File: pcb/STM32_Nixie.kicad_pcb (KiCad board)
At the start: 4 copper layers, 154 x 57 mm, 189 parts, among them J1 CON_SAMTEC_14P_2R_1m27_P_KEY_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, J2 CONN_USBC_RCPT_USB2.0_USB4085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, Q1 NFET_250V_10A_TPH1110FNH,L1Q, Q2 NFET_60V_0A5_2N7002KT1G, SW1 ENC_SPST_24PPR_PEC12R-4225F-S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, U1 IC_SR_MC_HV5622PG-G, U2 IC_SR_MC_HV5622PG-G, U3 IC_MCU_STM32F100C4T6B_48LQFP, U4 IC_LVL_ONSEMI_MC14504BDTR2G, U5 REG_SW_BOOST_TI_TLV61046ADBV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

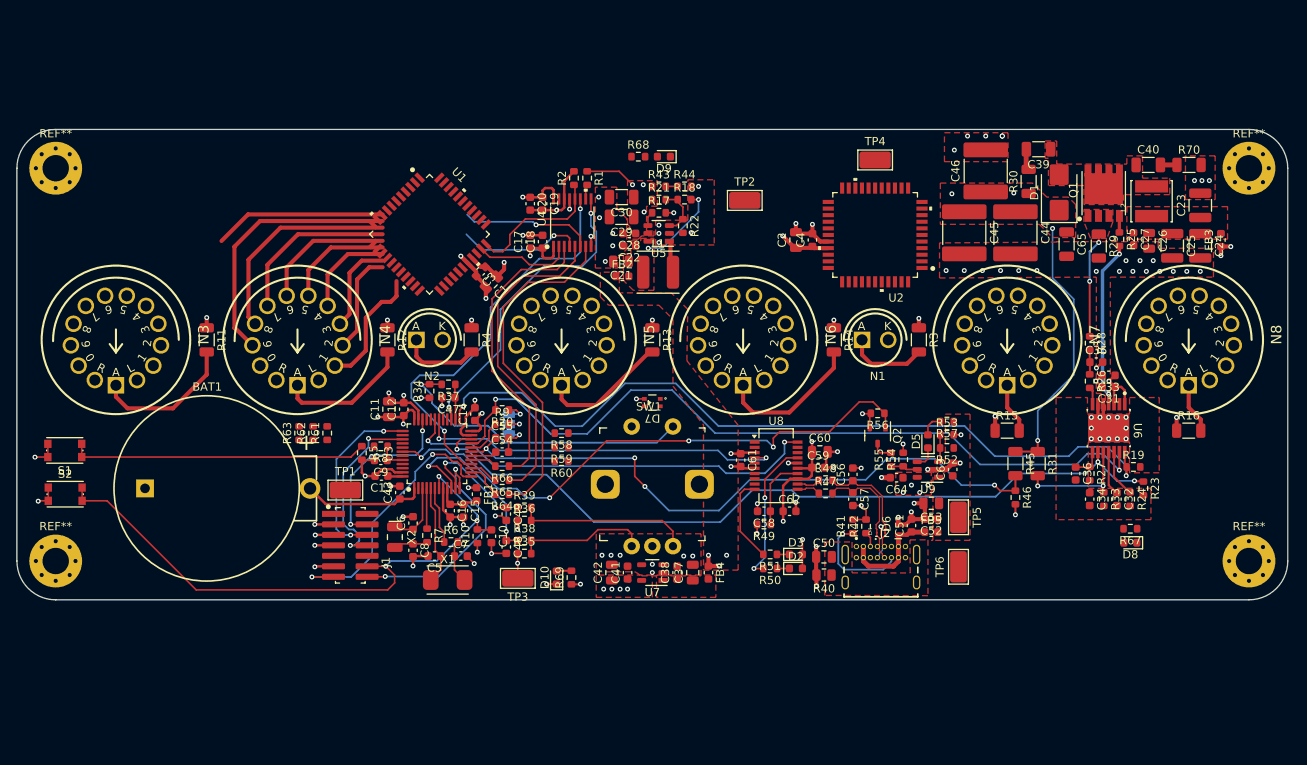
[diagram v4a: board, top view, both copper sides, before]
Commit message: Reshuffled nixie schematic to ease with routing. Need to fix the other 3 digits next.
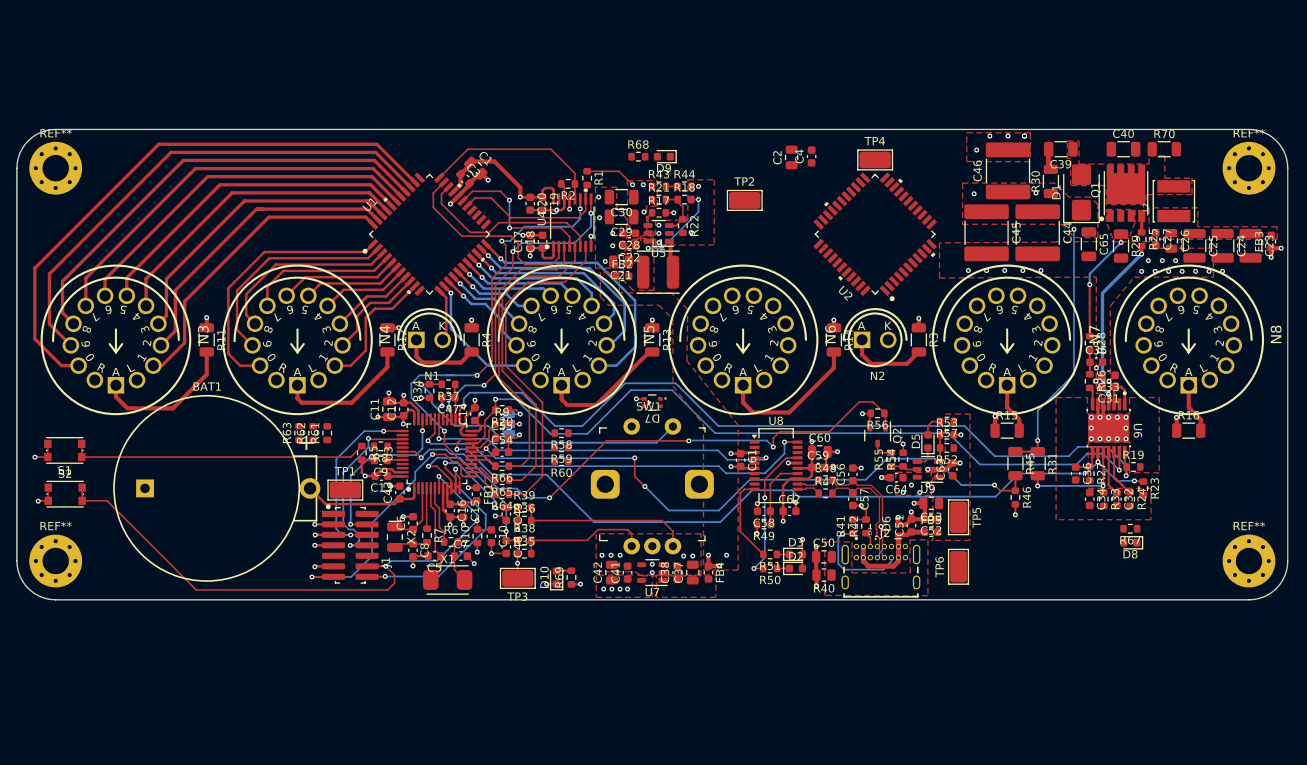
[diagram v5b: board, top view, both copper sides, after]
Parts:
- moved C1 13.9 mm to (130.6, 66.2), turned to -45 degrees
- moved C3 11.4 mm to (129.3, 67.5), turned to -45 degrees
- moved C4 10.1 mm to (171.3, 64.8)
- moved C2 10.0 mm to (168.9, 64.9)
- moved C23 7.82 mm to (224.5, 75.6), turned to -90 degrees
- moved FB3 6.10 mm to (227.0, 75.1)
- moved C40 3.55 mm to (209.1, 63.9)
- moved R70 3.55 mm to (214.0, 63.9)
- moved C26 2.70 mm to (214.9, 75.0)
- moved C65 2.70 mm to (204.9, 75.4)
- moved Q1 2.70 mm to (209.4, 69.2)
- moved R25 2.70 mm to (211.3, 74.8)
- moved R29 2.70 mm to (208.8, 75.6)
- moved R30 2.70 mm to (200.3, 67.8)
- moved C24 2.70 mm to (221.1, 75.6)
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- renumbered N2 to N1, N1 to N2
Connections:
- N1 pad A: /Nixie Display/DOT2_A -> /Nixie Display/DOT1_A
- N1 pad K: /Nixie Display/DOT2 -> /Nixie Display/DOT1
- N2 pad A: /Nixie Display/DOT1_A -> /Nixie Display/DOT2_A
- N2 pad K: /Nixie Display/DOT1 -> /Nixie Display/DOT2
- R3 pad 2: /Nixie Display/DOT1_A -> /Nixie Display/DOT2_A
- R4 pad 2: /Nixie Display/DOT2_A -> /Nixie Display/DOT1_A
- U1 pad 1: /Nixie Display/M1_2 -> /Nixie Display/H2_0
- U1 pad 10: /Nixie Display/H2_3 -> /Nixie Display/H2_1
- U1 pad 11: /Nixie Display/H2_2 -> unconnected-(U1-HVOUT12-Pad11)
- U1 pad 12: /Nixie Display/H2_1 -> /Nixie Display/DOT1
- U1 pad 13: /Nixie Display/H1_0 -> /Nixie Display/M1_0
- U1 pad 14: /Nixie Display/H1_9 -> /Nixie Display/M1_9
- U1 pad 15: /Nixie Display/H1_8 -> /Nixie Display/M1_8
- U1 pad 16: /Nixie Display/H1_7 -> /Nixie Display/M1_7
- U1 pad 17: /Nixie Display/H1_6 -> /Nixie Display/M1_6
- U1 pad 18: /Nixie Display/H1_5 -> /Nixie Display/M1_5
- U1 pad 19: /Nixie Display/H1_4 -> /Nixie Display/M1_4
- U1 pad 2: /Nixie Display/M1_1 -> /Nixie Display/H2_9
- U1 pad 20: /Nixie Display/H1_3 -> /Nixie Display/M1_3
- U1 pad 21: /Nixie Display/H1_2 -> /Nixie Display/M1_2
- U1 pad 22: /Nixie Display/H1_1 -> /Nixie Display/M1_1
- U1 pad 3: /Nixie Display/H2_0 -> /Nixie Display/H2_8
- U1 pad 35: /Nixie Display/M2_2 -> /Nixie Display/H1_0
- U1 pad 36: /Nixie Display/M2_1 -> /Nixie Display/H1_9
- U1 pad 37: /Nixie Display/M1_0 -> /Nixie Display/H1_8
- U1 pad 38: /Nixie Display/M1_9 -> /Nixie Display/H1_7
- U1 pad 39: /Nixie Display/M1_8 -> /Nixie Display/H1_6
- U1 pad 4: /Nixie Display/H2_9 -> /Nixie Display/H2_7
- U1 pad 40: /Nixie Display/M1_7 -> /Nixie Display/H1_5
- U1 pad 41: /Nixie Display/M1_6 -> /Nixie Display/H1_4
- U1 pad 42: /Nixie Display/M1_5 -> /Nixie Display/H1_3
- U1 pad 43: /Nixie Display/M1_4 -> /Nixie Display/H1_2
- U1 pad 44: /Nixie Display/M1_3 -> /Nixie Display/H1_1
- U1 pad 5: /Nixie Display/H2_8 -> /Nixie Display/H2_6
- U1 pad 6: /Nixie Display/H2_7 -> /Nixie Display/H2_5
- U1 pad 7: /Nixie Display/H2_6 -> /Nixie Display/H2_4
- U1 pad 8: /Nixie Display/H2_5 -> /Nixie Display/H2_3
- U1 pad 9: /Nixie Display/H2_4 -> /Nixie Display/H2_2
- U2 pad 1: /Nixie Display/S2_4 -> /Nixie Display/S2_2
- U2 pad 10: /Nixie Display/S1_5 -> /Nixie Display/S1_3
- U2 pad 11: /Nixie Display/S1_4 -> /Nixie Display/S1_2
- U2 pad 12: /Nixie Display/S1_3 -> /Nixie Display/S1_1
- U2 pad 13: /Nixie Display/S1_2 -> /Nixie Display/M2_0
- U2 pad 14: /Nixie Display/S1_1 -> /Nixie Display/M2_9
- U2 pad 15: /Nixie Display/M2_0 -> /Nixie Display/M2_8
- U2 pad 16: /Nixie Display/M2_9 -> /Nixie Display/M2_7
- U2 pad 17: /Nixie Display/M2_8 -> /Nixie Display/M2_6
- U2 pad 18: /Nixie Display/M2_7 -> /Nixie Display/M2_5
- U2 pad 19: /Nixie Display/M2_6 -> /Nixie Display/M2_4
- U2 pad 2: /Nixie Display/S2_3 -> /Nixie Display/S2_1
- U2 pad 20: /Nixie Display/M2_5 -> /Nixie Display/M2_3
- U2 pad 21: /Nixie Display/M2_4 -> /Nixie Display/M2_2
- U2 pad 22: /Nixie Display/M2_3 -> /Nixie Display/M2_1
- U2 pad 3: /Nixie Display/S2_2 -> /Nixie Display/S1_0
- U2 pad 35: unconnected-(U2-HVOUT32-Pad35) -> /Nixie Display/DOT2
- U2 pad 37: /Nixie Display/DOT2 -> /Nixie Display/S2_0
- U2 pad 38: /Nixie Display/DOT1 -> /Nixie Display/S2_9
- U2 pad 39: /Nixie Display/S2_0 -> /Nixie Display/S2_8
- U2 pad 4: /Nixie Display/S2_1 -> /Nixie Display/S1_9
- U2 pad 40: /Nixie Display/S2_9 -> /Nixie Display/S2_7
- U2 pad 41: /Nixie Display/S2_8 -> /Nixie Display/S2_6
- U2 pad 42: /Nixie Display/S2_7 -> /Nixie Display/S2_5
- U2 pad 43: /Nixie Display/S2_6 -> /Nixie Display/S2_4
- U2 pad 44: /Nixie Display/S2_5 -> /Nixie Display/S2_3
- U2 pad 5: /Nixie Display/S1_0 -> /Nixie Display/S1_8
- U2 pad 6: /Nixie Display/S1_9 -> /Nixie Display/S1_7
- U2 pad 7: /Nixie Display/S1_8 -> /Nixie Display/S1_6
- U2 pad 8: /Nixie Display/S1_7 -> /Nixie Display/S1_5
- U2 pad 9: /Nixie Display/S1_6 -> /Nixie Display/S1_4
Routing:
- net /Nixie Display/H1_0: track 0.00 -> 69.4 mm
- net /Nixie Display/H1_9: track 0.00 -> 61.3 mm
- net /Nixie Display/H1_8: track 0.00 -> 54.9 mm
- net /Nixie Display/H1_7: track 0.00 -> 48.5 mm
- net /Nixie Display/H1_6: track 0.00 -> 43.7 mm
- net /Nixie Display/H1_5: track 0.00 -> 40.0 mm
- net /Nixie Display/H1_4: track 0.00 -> 37.7 mm
- net /Nixie Display/H1_1: track 0.00 -> 37.4 mm
- net /Nixie Display/H1_2: track 0.00 -> 36.9 mm
- net /Nixie Display/H1_3: track 0.00 -> 36.6 mm
- net /Nixie Display/M1_1: track 0.00 -> 31.8 mm, vias 0 -> 1
- net /Nixie Display/M1_2: track 0.00 -> 26.4 mm, vias 0 -> 1
- net /Nixie Display/M1_3: track 0.00 -> 22.1 mm, vias 0 -> 1
- net /Nixie Display/M1_4: track 0.00 -> 17.8 mm, vias 0 -> 1
- net /nPOL_12V: track 1.77 -> 19.3 mm
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
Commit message: Reshuffled Nixie page some more to make routing cleaner
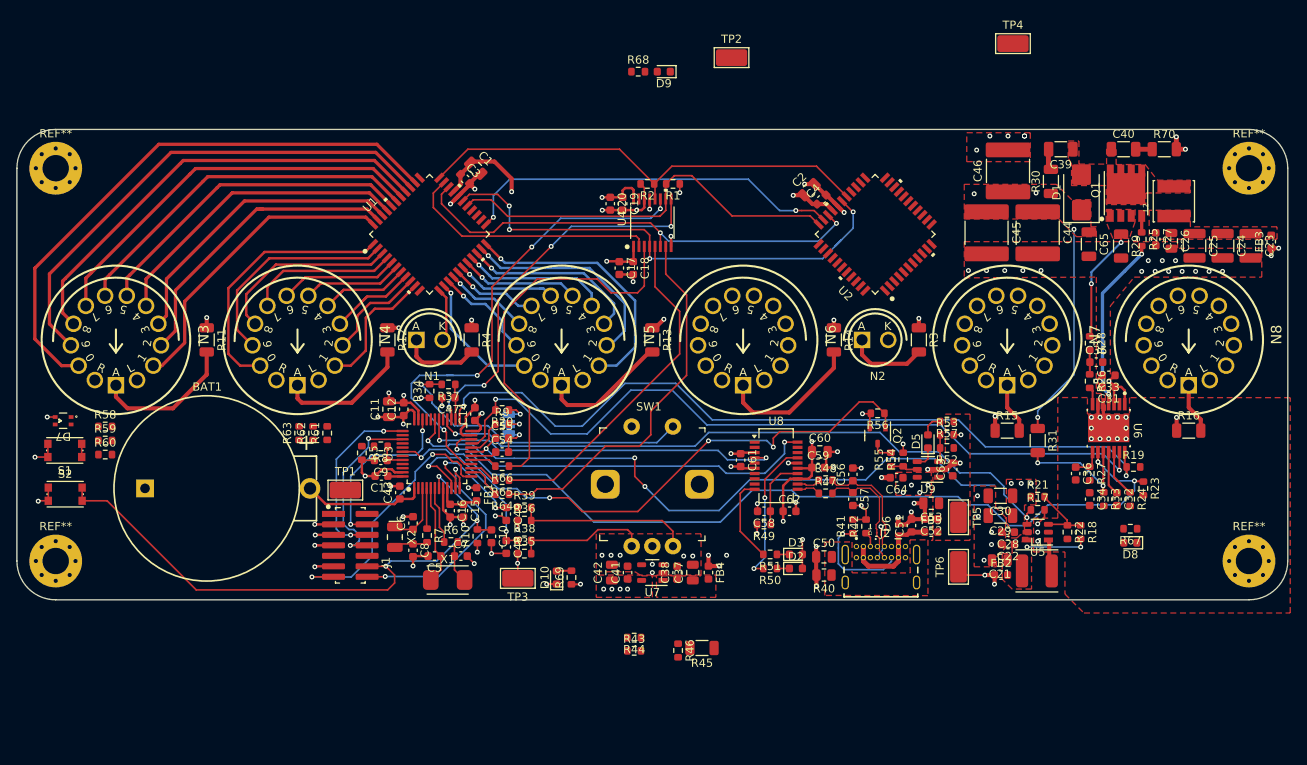
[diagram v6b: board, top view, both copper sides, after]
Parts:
- moved D7 71.4 mm to (80.6, 96.8)
- moved R18 62.7 mm to (203.9, 110.3), turned to -90 degrees
- moved R22 59.6 mm to (202.3, 110.3)
- moved U5 58.5 mm to (198.7, 110.3)
- moved C28 58.5 mm to (195.1, 110.3)
- moved C21 58.5 mm to (194.1, 113.7)
- moved C22 58.5 mm to (195.1, 111.8)
- moved C29 58.5 mm to (194.2, 108.3)
- moved C30 58.5 mm to (194.2, 105.9)
- moved L1 58.5 mm to (198.6, 115.0)
- moved FB2 58.5 mm to (194.3, 115.5)
- moved R17 58.3 mm to (198.7, 107.6)
- moved R21 58.3 mm to (198.7, 106.0)
- moved R43 56.4 mm to (149.8, 124.7)
- moved R58 55.3 mm to (85.7, 97.5), turned to 0 degrees
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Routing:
- net +12V: track 120.8 -> 31.6 mm, vias 5 -> 8
- net /MCU/EN_12V: track 1.76 -> 79.6 mm, vias 0 -> 2
- net /Nixie Display/DATA_CHAIN: track 0.00 -> 46.7 mm, vias 0 -> 2
- net /SPI_SCK_12V: track 18.9 -> 62.1 mm, vias 2 -> 4
- net /PWM_nBL_12V: track 22.2 -> 56.8 mm
- net /MCU/BOOT0_SW: track 36.1 -> 1.60 mm
- net /SPI_nCS_nLE_12V: track 23.0 -> 57.1 mm, vias 0 -> 2
- net /nPOL_12V: track 19.3 -> 50.0 mm
- net /SPI_PICO_3V3: track 35.9 -> 46.3 mm
- net GND: track 128.1 -> 136.5 mm
- net /MCU/DITHOFF_180V: track 95.3 -> 102.4 mm
- net /SPI_PICO_12V: track 24.4 -> 31.0 mm
- net /PWM_nBL_3V3: track 53.4 -> 59.5 mm
- net /nPOL_3V3: track 40.7 -> 46.4 mm
- net +5V: track 4.94 -> 10.3 mm, vias 9 -> 11
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
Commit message: All nets routed!! (I think)
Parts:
- moved R45 40.4 mm to (183.4, 92.9)
- moved R46 39.8 mm to (179.1, 92.9), turned to 180 degrees
- moved TP4 35.3 mm to (162.8, 64.0)
- moved R43 30.1 mm to (153.6, 94.8), turned to 180 degrees
- moved R44 28.3 mm to (150.4, 94.8)
- moved TP2 25.6 mm to (142.7, 70.0)
- moved D9 22.0 mm to (137.8, 70.0), turned to -90 degrees
- moved R68 18.9 mm to (139.5, 70.0), turned to -90 degrees
- moved D8 12.5 mm to (219.4, 103.4)
- moved R67 9.03 mm to (216.2, 103.4), turned to 0 degrees
- moved S1 2.70 mm to (80.9, 103.1)
- moved D7 2.32 mm to (80.9, 99.1)
- moved S2 1.40 mm to (80.9, 107.1)
- moved R61 1.30 mm to (113.7, 99.0)
- moved R62 1.30 mm to (112.0, 99.0)
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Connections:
- U2 pad 1: /Nixie Display/S2_2 -> /Nixie Display/DOT2
- U2 pad 10: /Nixie Display/S1_3 -> /Nixie Display/S1_2
- U2 pad 11: /Nixie Display/S1_2 -> /Nixie Display/S1_1
- U2 pad 12: /Nixie Display/S1_1 -> unconnected-(U2-HVOUT11-Pad12)
- U2 pad 13: /Nixie Display/M2_0 -> /Nixie Display/S2_0
- U2 pad 14: /Nixie Display/M2_9 -> /Nixie Display/S2_9
- U2 pad 15: /Nixie Display/M2_8 -> /Nixie Display/S2_8
- U2 pad 16: /Nixie Display/M2_7 -> /Nixie Display/S2_7
- U2 pad 17: /Nixie Display/M2_6 -> /Nixie Display/S2_6
- U2 pad 18: /Nixie Display/M2_5 -> /Nixie Display/S2_5
- U2 pad 19: /Nixie Display/M2_4 -> /Nixie Display/S2_4
- U2 pad 2: /Nixie Display/S2_1 -> /Nixie Display/S1_0
- U2 pad 20: /Nixie Display/M2_3 -> /Nixie Display/S2_3
- U2 pad 21: /Nixie Display/M2_2 -> /Nixie Display/S2_2
- U2 pad 22: /Nixie Display/M2_1 -> /Nixie Display/S2_1
- U2 pad 3: /Nixie Display/S1_0 -> /Nixie Display/S1_9
- U2 pad 35: /Nixie Display/DOT2 -> /Nixie Display/M2_0
- U2 pad 36: unconnected-(U2-HVOUT31-Pad36) -> /Nixie Display/M2_9
- U2 pad 37: /Nixie Display/S2_0 -> /Nixie Display/M2_8
- U2 pad 38: /Nixie Display/S2_9 -> /Nixie Display/M2_7
- U2 pad 39: /Nixie Display/S2_8 -> /Nixie Display/M2_6
- U2 pad 4: /Nixie Display/S1_9 -> /Nixie Display/S1_8
- U2 pad 40: /Nixie Display/S2_7 -> /Nixie Display/M2_5
- U2 pad 41: /Nixie Display/S2_6 -> /Nixie Display/M2_4
- U2 pad 42: /Nixie Display/S2_5 -> /Nixie Display/M2_3
- U2 pad 43: /Nixie Display/S2_4 -> /Nixie Display/M2_2
- U2 pad 44: /Nixie Display/S2_3 -> /Nixie Display/M2_1
- U2 pad 5: /Nixie Display/S1_8 -> /Nixie Display/S1_7
- U2 pad 6: /Nixie Display/S1_7 -> /Nixie Display/S1_6
- U2 pad 7: /Nixie Display/S1_6 -> /Nixie Display/S1_5
- U2 pad 8: /Nixie Display/S1_5 -> /Nixie Display/S1_4
- U2 pad 9: /Nixie Display/S1_4 -> /Nixie Display/S1_3
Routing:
- net /Nixie Display/S2_1: track 0.00 -> 67.0 mm, vias 0 -> 1
- net /Nixie Display/S2_8: track 0.00 -> 63.0 mm, vias 0 -> 1
- net /Nixie Display/S2_9: track 0.00 -> 60.7 mm, vias 0 -> 1
- net /Nixie Display/S2_2: track 0.00 -> 60.5 mm, vias 0 -> 1
- net /Nixie Display/S2_0: track 0.00 -> 58.5 mm, vias 0 -> 1
- net /Nixie Display/S2_3: track 0.00 -> 54.3 mm, vias 0 -> 1
- net /Nixie Display/S2_4: track 0.00 -> 49.7 mm, vias 0 -> 1
- net /MCU/HW_REV1: track 0.00 -> 45.4 mm, vias 0 -> 2
- net /Nixie Display/S2_5: track 0.00 -> 45.1 mm, vias 0 -> 1
- net /Nixie Display/S2_6: track 0.00 -> 43.7 mm, vias 0 -> 1
- net /MCU/LED_BLUE: track 0.00 -> 43.4 mm, vias 0 -> 2
- net /MCU/LED_RED: track 0.00 -> 43.2 mm, vias 0 -> 2
- net /Nixie Display/S2_7: track 0.00 -> 39.2 mm, vias 0 -> 1
- net /MCU/HW_REV0: track 0.00 -> 37.8 mm, vias 0 -> 2
- net /MCU/LED_GREEN: track 0.00 -> 36.7 mm
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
